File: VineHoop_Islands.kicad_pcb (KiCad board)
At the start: 2 copper layers, 49.3 x 15.2 mm, 31 parts, among them J1 95278-101A04LF, J2 20021121-00006C4LF, J3 20021121-00006C4LF, U1 MIC5205-3.3YM5, U2 SHT31-DIS-B, U3 BNO055, U4 ATMEGA328P-MUR, Y1 ABS07-32.768KHZ-T, Y2 ABM10-16.000MHZ-E20-T

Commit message: Monday evening commit
I know this is not how I’m supposed to use Git
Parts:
- removed J3: 20021121-00006C4LF, 6pin:Amphenol_ICC___FCI-20021121-00006C4LF-MFG
- moved J1 73.9 mm to (102.6, 81.5)
- moved R2 72.1 mm to (219.1, 81.6), turned to -90 degrees
- moved U2 65.6 mm to (215.9, 81.6), turned to 180 degrees
- moved R3 59.5 mm to (212.6, 81.6), turned to -90 degrees
- moved Y1 36.4 mm to (189.6, 84.8), turned to 180 degrees
- moved C1 34.3 mm to (191.2, 82.8), turned to 0 degrees
- moved R1 33.0 mm to (184.8, 83.2), turned to -90 degrees
- moved C2 32.9 mm to (187.4, 82.8), turned to 180 degrees
- moved R5 30.6 mm to (191.7, 78.6)
- moved C6 30.5 mm to (191.6, 80.3)
- moved R4 28.7 mm to (182.5, 80.2), turned to -90 degrees
- moved U3 27.7 mm to (186.7, 79.2), turned to 180 degrees
- moved R7 25.3 mm to (190.8, 76.0), turned to 90 degrees
- moved C4 23.9 mm to (188.3, 76.0), turned to 0 degrees
- moved R8 23.5 mm to (182.4, 77.1), turned to 90 degrees
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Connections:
- J2 pad 1: Net-(J2-Pad1) -> RESET
- J2 pad 2: RX -> SCK
- J2 pad 4: VDD -> MOSI
- J2 pad 5: Net-(J2-Pad5) -> RX
- J2 pad 6: GND -> MISO
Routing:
- net VDD: track 48.3 -> 10.5 mm
- net TX: track 42.1 -> 13.1 mm, vias 2 -> 0
- net Net-(R11-Pad2): track 2.52 -> 28.7 mm, vias 0 -> 2
- net RX: track 32.7 -> 12.0 mm, vias 2 -> 0
- net RESET: track 26.6 -> 13.2 mm
- net +3V3: track 121.3 -> 134.7 mm, vias 0 -> 2
- net MISO: track 14.7 -> 5.33 mm
- net SENSOR_SCL: track 32.7 -> 24.2 mm, vias 2 -> 0
- net SCL: track 29.2 -> 21.9 mm
- net SDA: track 25.2 -> 22.2 mm
- net SENSOR_SDA: track 24.1 -> 26.9 mm, vias 2 -> 0
- net SCK: track 11.2 -> 8.47 mm
- net GND: track 64.7 -> 62.0 mm, vias 30 -> 25
- net Net-(R3-Pad2): track 4.42 -> 2.58 mm
- net Net-(C9-Pad2): track 8.82 -> 10.2 mm, vias 0 -> 2
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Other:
- board outline removed

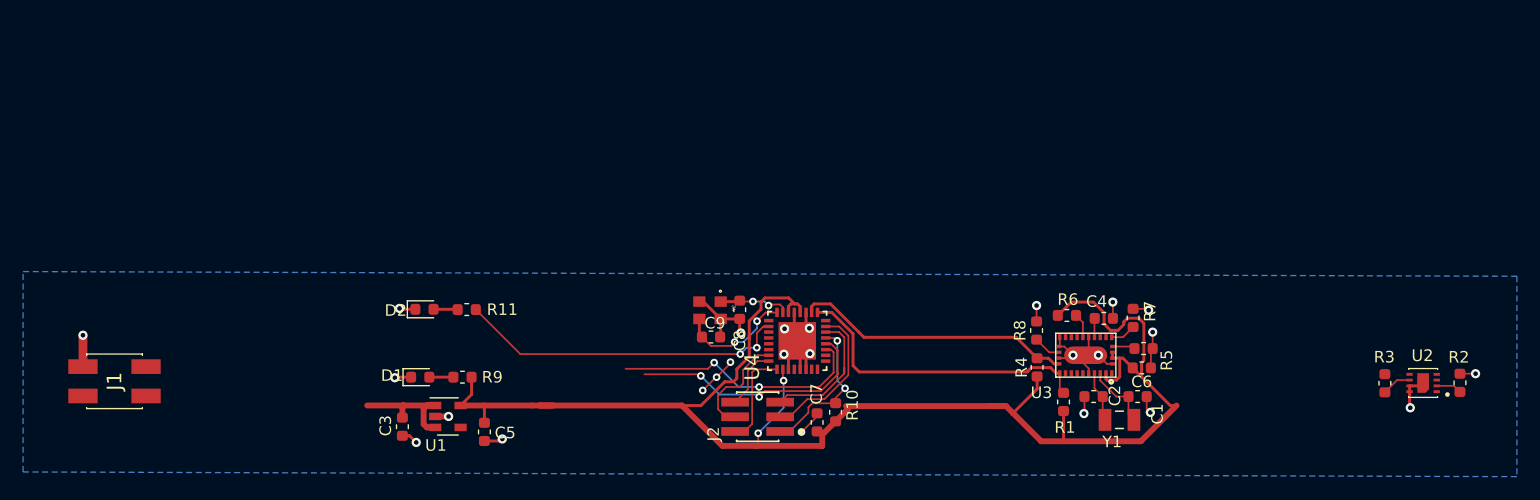
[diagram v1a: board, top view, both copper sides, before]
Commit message: First rough draft of islands
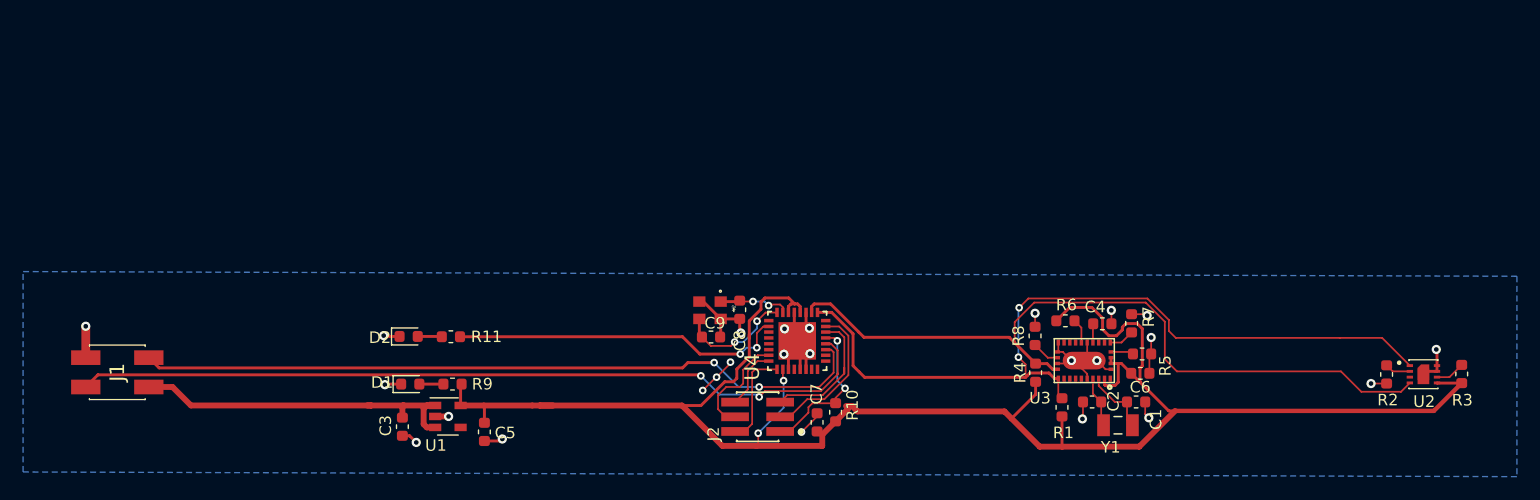
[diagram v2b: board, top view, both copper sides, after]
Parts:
- moved R3 6.70 mm to (219.2, 80.8), turned to 90 degrees
- moved R2 6.39 mm to (212.8, 80.9), turned to 90 degrees
- moved D2 2.72 mm to (128.1, 77.6)
- moved R11 2.72 mm to (131.8, 77.6)
- moved D1 1.05 mm to (128.2, 81.7)
- moved R9 1.05 mm to (131.9, 81.7)
- moved J1 0.81 mm to (102.9, 80.7)
- moved U2 0.76 mm to (215.9, 80.8), turned to 0 degrees
- moved C2 0.48 mm to (187.3, 83.2)
- moved C1 0.48 mm to (191.1, 83.2)
- moved C6 0.48 mm to (191.4, 80.8)
- moved U3 0.48 mm to (186.6, 79.7)
- moved R6 0.48 mm to (184.9, 76.2)
- moved C4 0.48 mm to (188.1, 76.5)
- moved R1 0.48 mm to (184.7, 83.7)
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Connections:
- J1 pad 2: SCL -> SDA
- J1 pad 3: SDA -> SCL
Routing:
- net SCL: track 21.9 -> 70.9 mm
- net SENSOR_SDA: track 26.9 -> 70.4 mm, vias 0 -> 2
- net SENSOR_SCL: track 24.2 -> 66.4 mm
- net SDA: track 22.2 -> 63.8 mm
- net +3V3: track 134.7 -> 160.6 mm
- net VDD: track 10.5 -> 30.4 mm

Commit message: Minor edits
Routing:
- net +3V3: track 160.6 -> 159.9 mm
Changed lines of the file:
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@@
     (thickness 1.6)
     (drawings 84)
-    (tracks 386)
+    (tracks 383)
     (modules 30)
     (nets 42)
@@
   (segment (start 132.588899 81.786101) (end 132.675 81.7) (width 0.254) (layer "F.Cu") (net 4))
   (segment (start 134.65 85.05) (end 134.65 83.6) (width 0.254) (layer "F.Cu") (net 4))
-  (segment (start 166.1 83.6) (end 166.479195 83.6) (width 0.508) (layer "F.Cu") (net 4))
-  (segment (start 166.479195 83.6) (end 166.945245 84.06605) (width 0.508) (layer "F.Cu") (net 4))
   (segment (start 182.719931 87.11605) (end 184.6692 87.11605) (width 0.508) (layer "F.Cu") (net 4))
   (segment (start 184.6692 87.11605) (end 191.339815 87.11605) (width 0.508) (layer "F.Cu") (net 4))
@@
   (segment (start 182.364 81.50195) (end 182.364 82.595451) (width 0.254) (layer "F.Cu") (net 4))
   (segment (start 156.2 81.5) (end 156.5 81.2) (width 0.254) (layer "F.Cu") (net 4))
+  (segment (start 165.05 84.925) (end 166.086295 84.925) (width 0.508) (layer "F.Cu") (net 4))
+  (segment (start 166.086295 84.925) (end 166.945245 84.06605) (width 0.508) (layer "F.Cu") (net 4))
   (segment (start 158.592799 75.215457) (end 158.592799 74.584543) (width 0.254) (layer "F.Cu") (net 4))
   (segment (start 157.577001 79.322999) (end 157.577001 77.427001) (width 0.254) (layer "F.Cu") (net 4))
   (segment (start 190.188018 76.46044) (end 191.159982 76.46044) (width 0.254) (layer "F.Cu") (net 4))
   (segment (start 189.240601 81.816951) (end 189.5181 81.539452) (width 0.254) (layer "F.Cu") (net 4))
-  (segment (start 165.05 84.925) (end 166.1 83.875) (width 0.508) (layer "F.Cu") (net 4))
   (segment (start 191.159982 76.46044) (end 191.60279 76.903248) (width 0.254) (layer "F.Cu") (net 4))
   (segment (start 179.669931 84.06605) (end 182.719931 87.11605) (width 0.508) (layer "F.Cu") (net 4))
@@
   (segment (start 158.934543 74.242799) (end 160.992799 74.242799) (width 0.254) (layer "F.Cu") (net 4))
   (segment (start 219.25 81.6125) (end 217.1266 81.6125) (width 0.254) (layer "F.Cu") (net 4))
-  (segment (start 166.1 83.875) (end 166.1 83.6) (width 0.508) (layer "F.Cu") (net 4))
-  (segment (start 166.1 83.6) (end 165.954031 83.6) (width 0.508) (layer "F.Cu") (net 4))
   (via (at 160.55 81.4) (size 0.6604) (drill 0.3302) (layers "F.Cu" "B.Cu") (net 4))
   (via (at 158.35 85.95) (size 0.6604) (drill 0.3302) (layers "F.Cu" "B.Cu") (net 4))
@@
     (connect_pads (clearance 0.254))
     (min_thickness 0.254)
-    (fill yes (mode hatch) (thermal_gap 0.254) (thermal_bridge_width 0.254)
-      (hatch_thickness 0.254) (hatch_gap 0.254) (hatch_orientation 45))
+    (fill yes (thermal_gap 0.254) (thermal_bridge_width 0.254))
     (polygon
       (pts

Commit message: Big backup
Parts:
- removed Y2: ABM10-16.000MHZ-E20-T, ABM10-16.000MHZ-E20-T:XTAL250X200X50
- added R12: 10K, Resistor_SMD:R_0603_1608Metric, F.Cu at (131.6, 80.2)
- added R13: 10K, Resistor_SMD:R_0603_1608Metric, F.Cu at (157.8, 80.1)
- added R14: 10K, Resistor_SMD:R_0603_1608Metric, F.Cu at (188.6, 80.2)
- added R15: 10K, Resistor_SMD:R_0603_1608Metric, F.Cu at (217.1, 80.2)
- added TH1: 10K, Resistor_SMD:R_0603_1608Metric, F.Cu at (128.3, 80.2)
- added TH2: 10K, Resistor_SMD:R_0603_1608Metric, F.Cu at (160.9, 80.1)
- added TH3: 10K, Resistor_SMD:R_0603_1608Metric, F.Cu at (191.9, 80.2)
- added TH4: 10K, Resistor_SMD:R_0603_1608Metric, F.Cu at (220.3, 80.2)
- C8: value 22pF -> 0.1uF
- C9: value 22pF -> 10uF
- moved C9 68.3 mm to (221.1, 63.3), turned to 0 degrees
- moved C8 66.0 mm to (221.1, 60.6), turned to 180 degrees
- moved J1 37.5 mm to (130.0, 54.9)
- moved D2 37.5 mm to (155.7, 52.3)
- moved R11 37.5 mm to (159.4, 52.3)
- moved C7 32.5 mm to (164.0, 52.5), turned to 0 degrees
- moved J2 27.3 mm to (155.7, 57.3), turned to 0 degrees
- moved R3 23.2 mm to (222.3, 57.8)
- moved U2 23.2 mm to (219.0, 57.8)
- moved R2 23.2 mm to (215.8, 57.8)
- moved C6 22.8 mm to (194.5, 58.2)
- moved C1 22.8 mm to (194.1, 60.7)
- moved C2 22.8 mm to (190.3, 60.7)
- moved U3 22.8 mm to (189.7, 57.1)
- moved C4 22.8 mm to (191.2, 53.9)
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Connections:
- C8 pad 2: Net-(C8-Pad2) -> +3V3
- C9 pad 1: GND -> +3V3
- C9 pad 2: Net-(C9-Pad2) -> GND
- J1 pad 3: SCL -> VDD
- J1 pad 4: VDD -> SCL
- J2 pad 2: SCK -> MOSI
- J2 pad 4: MOSI -> MISO
- J2 pad 6: MISO -> SCK
- U4 pad 23: Net-(U4-Pad23) -> A0
- U4 pad 24: Net-(U4-Pad24) -> A1
- U4 pad 25: PC2 -> A2
- U4 pad 26: Net-(U4-Pad26) -> A3
- U4 pad 7: Net-(C8-Pad2) -> Net-(U4-Pad7)
- U4 pad 8: Net-(C9-Pad2) -> Net-(U4-Pad8)
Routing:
- net A3: track 0.00 -> 89.8 mm, vias 0 -> 4
- net +3V3: track 159.9 -> 243.6 mm
- net A2: track 0.00 -> 59.1 mm, vias 0 -> 2
- net A0: track 0.00 -> 54.6 mm, vias 0 -> 2
- net SCL: track 70.9 -> 34.1 mm
- net SDA: track 63.8 -> 34.1 mm
- net A1: track 0.00 -> 26.3 mm, vias 0 -> 2
- net Net-(R11-Pad2): track 29.1 -> 4.27 mm, vias 2 -> 0
- net VDD: track 30.4 -> 14.1 mm
- net Net-(C9-Pad2): track 10.2 -> 0.00 mm, vias 2 -> 0
- net Net-(C8-Pad2): track 6.48 -> 0.00 mm, vias 2 -> 0
- net SCK: track 8.47 -> 2.44 mm
- net GND: track 62.0 -> 57.1 mm, vias 25 -> 27
- net SENSOR_SCL: track 66.4 -> 69.6 mm, vias 0 -> 2
- net RX: track 12.0 -> 9.22 mm, vias 0 -> 2
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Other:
- board outline added: 98.5 x 30 mm
- board text added: "For Instructional Use Only."
- board text added: "SOLIDWORKS Educational Product."
